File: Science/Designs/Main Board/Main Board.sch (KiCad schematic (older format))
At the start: 26 parts

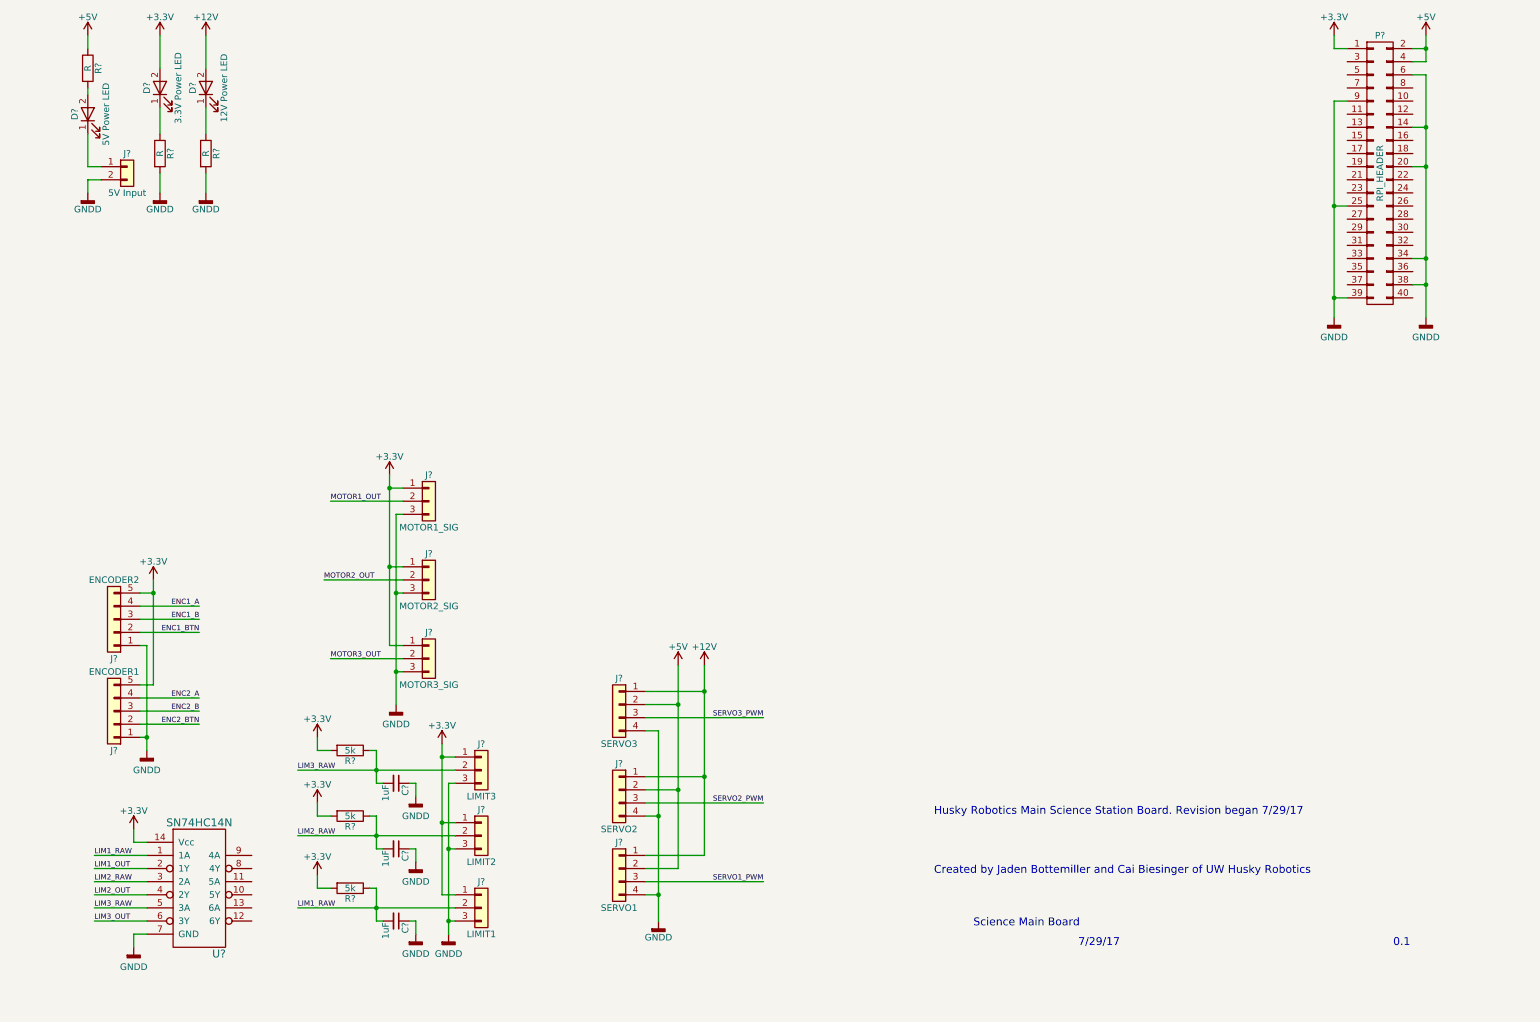
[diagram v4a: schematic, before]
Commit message: Changed LS7366R implementation per spec
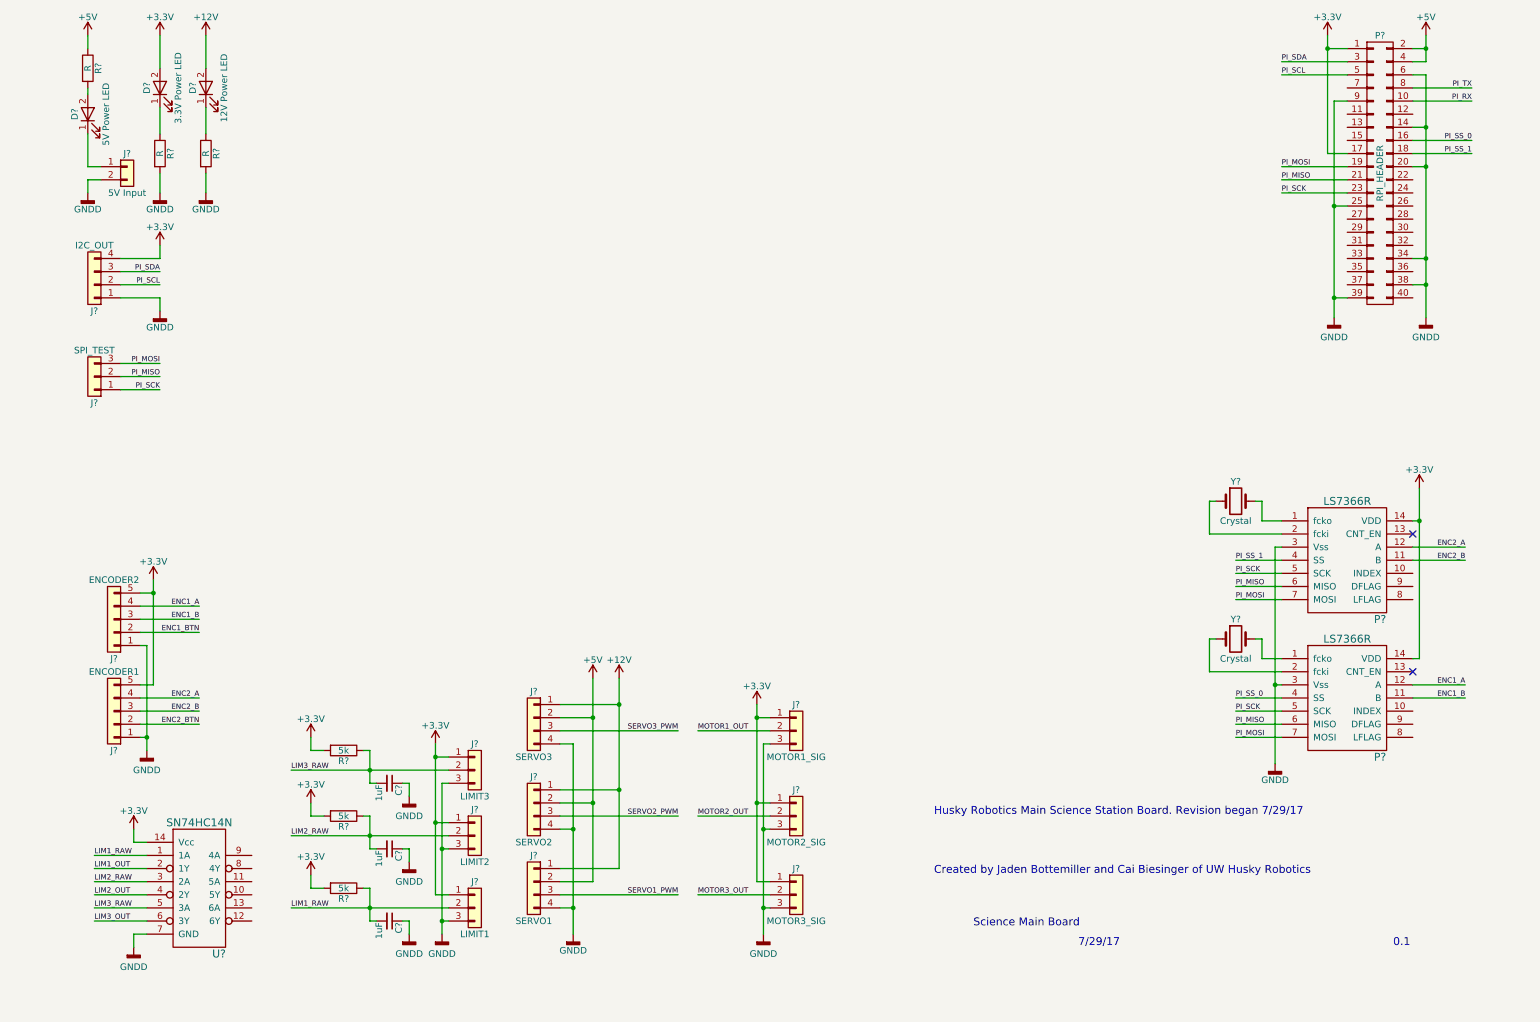
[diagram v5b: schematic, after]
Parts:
- added J?: I2C_OUT, symbol Conn_01x04
- added J?: SPI_TEST, symbol Conn_01x03
- added P? (x2): LS7366R, symbol LS7366R
- added Y? (x2): Crystal, symbol Crystal
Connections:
- net +3V3: now also P?.17 (P17), J?.4 (Pin_4), P?.14 (VDD), P?.14 (VDD)
- net ENC1_A: now also P?.12 (A)
- net ENC1_B: now also P?.11 (B)
- net ENC2_A: now also P?.12 (A)
- net ENC2_B: now also P?.11 (B)
- net GNDD: now also J?.1 (Pin_1), P?.3 (Vss), P?.3 (Vss)
- net PI_RX: now reaches P?.10 (P10)
- net PI_SS_0: now reaches P?.16 (P16)
- net PI_SS_0: now also P?.4 (SS)
- net PI_SS_1: now reaches P?.18 (P18)
- net PI_SS_1: now also P?.4 (SS)
- net PI_MOSI: now reaches P?.19 (P19)
- net PI_MOSI: now also J?.3 (Pin_3), P?.7 (MOSI), P?.7 (MOSI)
- net PI_MISO: now reaches P?.21 (P21)
- net PI_MISO: now also J?.2 (Pin_2), P?.6 (MISO), P?.6 (MISO)
- net PI_SCK: now reaches P?.23 (P23)
- net PI_SCK: now also J?.1 (Pin_1), P?.5 (SCK), P?.5 (SCK)
- net PI_SDA: now reaches P?.3 (P3)
- net PI_SDA: now also J?.3 (Pin_3)
- net PI_SCL: now reaches P?.5 (P5)
- net PI_SCL: now also J?.2 (Pin_2)
- net PI_TX: now reaches P?.8 (P8)
- new net: P?.1 (fcko), Y?.2 (x2)
- new net: P?.2 (fcki), Y?.1 (x2)
- no-connect marks 0 -> 2
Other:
- moved on the sheet: C?, J?, R?

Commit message: Added sensor connections
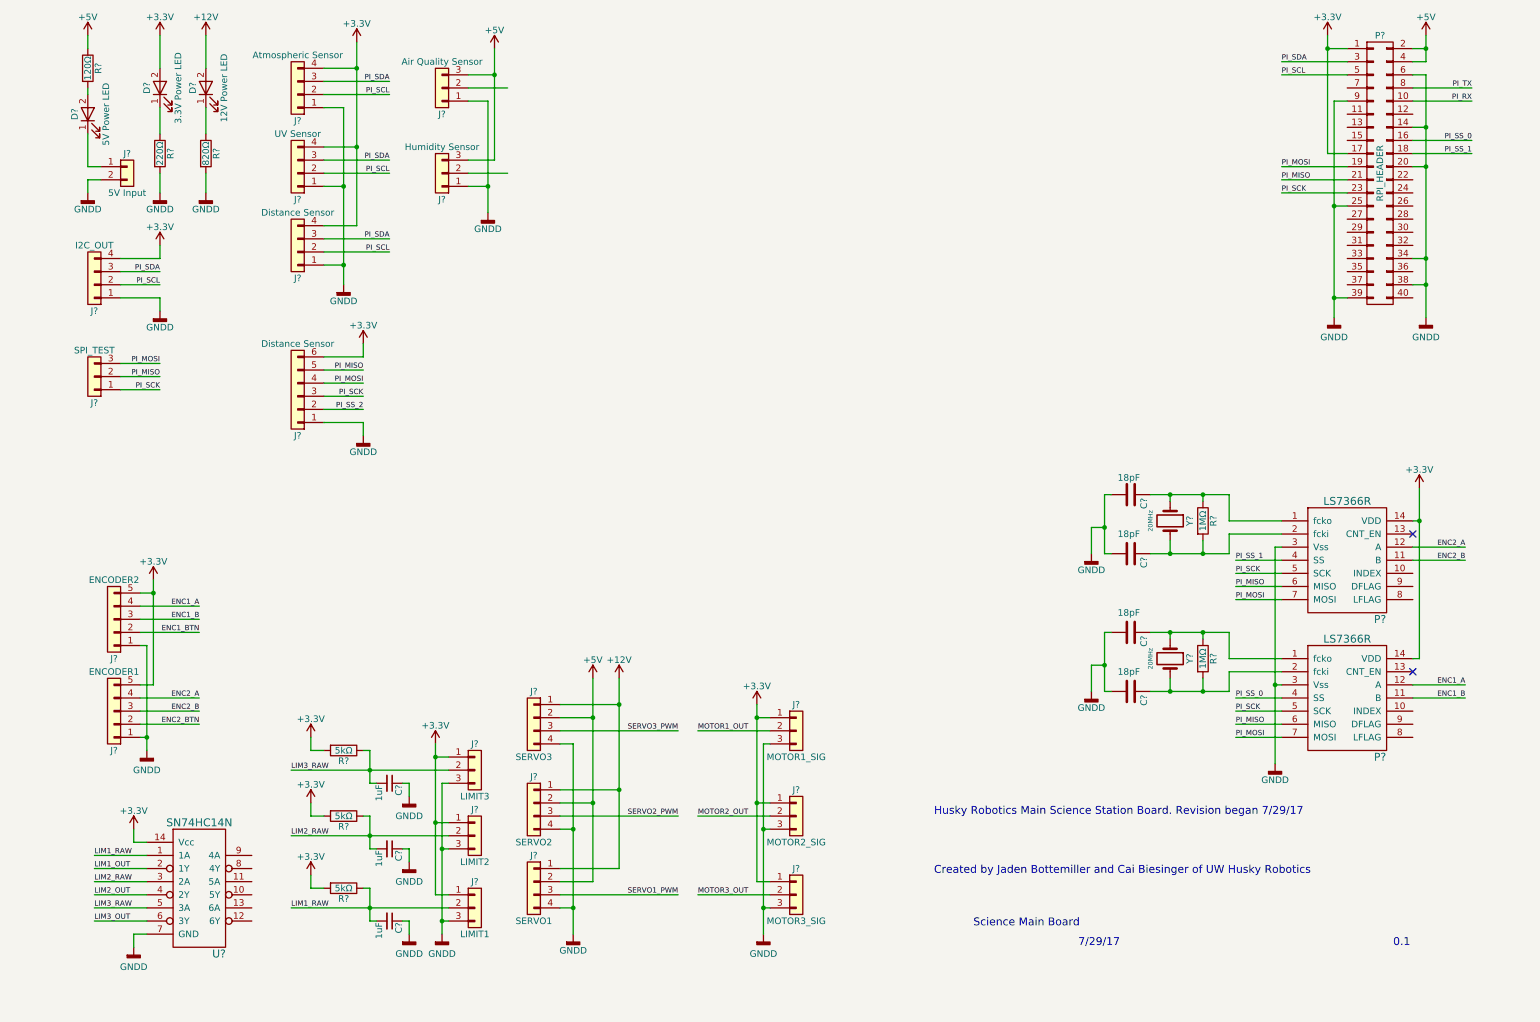
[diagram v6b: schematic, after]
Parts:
- removed Y? (x2): Crystal, symbol Crystal
- added C? (x4): 18pF, symbol C
- added J?: Atmospheric Sensor, symbol Conn_01x04
- added J?: UV Sensor, symbol Conn_01x04
- added J?: Distance Sensor, symbol Conn_01x04
- added J?: Distance Sensor, symbol Conn_01x06
- added J?: Air Quality Sensor, symbol Conn_01x03
- added J?: Humidity Sensor, symbol Conn_01x03
- added R? (x2): 1MΩ, symbol R
- added Y? (x2): 20MHz, symbol Crystal
- R? (x3): value 5k -> 5kΩ
- R?: value R -> 220Ω
- R?: value R -> 120Ω
- R?: value R -> 820Ω
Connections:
- net +3V3: now also J?.4 (Pin_4), J?.4 (Pin_4), J?.4 (Pin_4), J?.6 (Pin_6)
- net +5V: now also J?.3 (Pin_3), J?.3 (Pin_3)
- net GNDD: now also C?.2, C?.2, C?.2, C?.2, J?.1 (Pin_1), J?.1 (Pin_1), J?.1 (Pin_1), J?.1 (Pin_1), J?.1 (Pin_1), J?.1 (Pin_1)
- net PI_MISO: now also J?.5 (Pin_5)
- net PI_MOSI: now also J?.4 (Pin_4)
- net PI_SCK: now also J?.3 (Pin_3)
- net PI_SCL: now also J?.2 (Pin_2), J?.2 (Pin_2), J?.2 (Pin_2)
- net PI_SDA: now also J?.3 (Pin_3), J?.3 (Pin_3), J?.3 (Pin_3)
- net at P?.1 (fcko): now also C?.1, R?.1, Y?.1 (x2)
- net at P?.2 (fcki): now also C?.1, R?.2, Y?.2 (x2)
- new net PI_SS_2: J?.2 (Pin_2)

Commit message: Added ADC to main board schematic
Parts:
- added R? (x2): 330Ω, symbol R
- added R? (x2): 640Ω, symbol R
- added U?: TLV2544ID, symbol TLV2544ID
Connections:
- net +3V3: now also U?.10 (CSTART), U?.12 (PWDN), U?.4 (INT), U?.5 (Vcc)
- net GNDD: now also R?.1, R?.1, U?.11 (GND), U?.14 (REFM)
- net PI_MISO: now also U?.1 (MISO)
- net PI_MOSI: now also U?.2 (MOSI)
- net PI_SCK: now also U?.3 (SCLK)
- net PI_SS_2: now also P?.29 (P29)
- net PI_SS_3: now reaches P?.31 (P31)
- net PI_SS_3: now also U?.16 (CS)
- net at J?.2 (Pin_2): now also R?.2 (x2)
- new net AQ_SENS_OUT: R?.1, R?.2, U?.6 (A0)
- new net HUM_SENS_OUT: R?.1, R?.2, U?.7 (A1)
- no-connect marks 2 -> 4
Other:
- moved on the sheet: J?
